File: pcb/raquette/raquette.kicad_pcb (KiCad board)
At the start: 2 copper layers, 105 x 150 mm, 17 parts, among them U1 Teensy 4.1

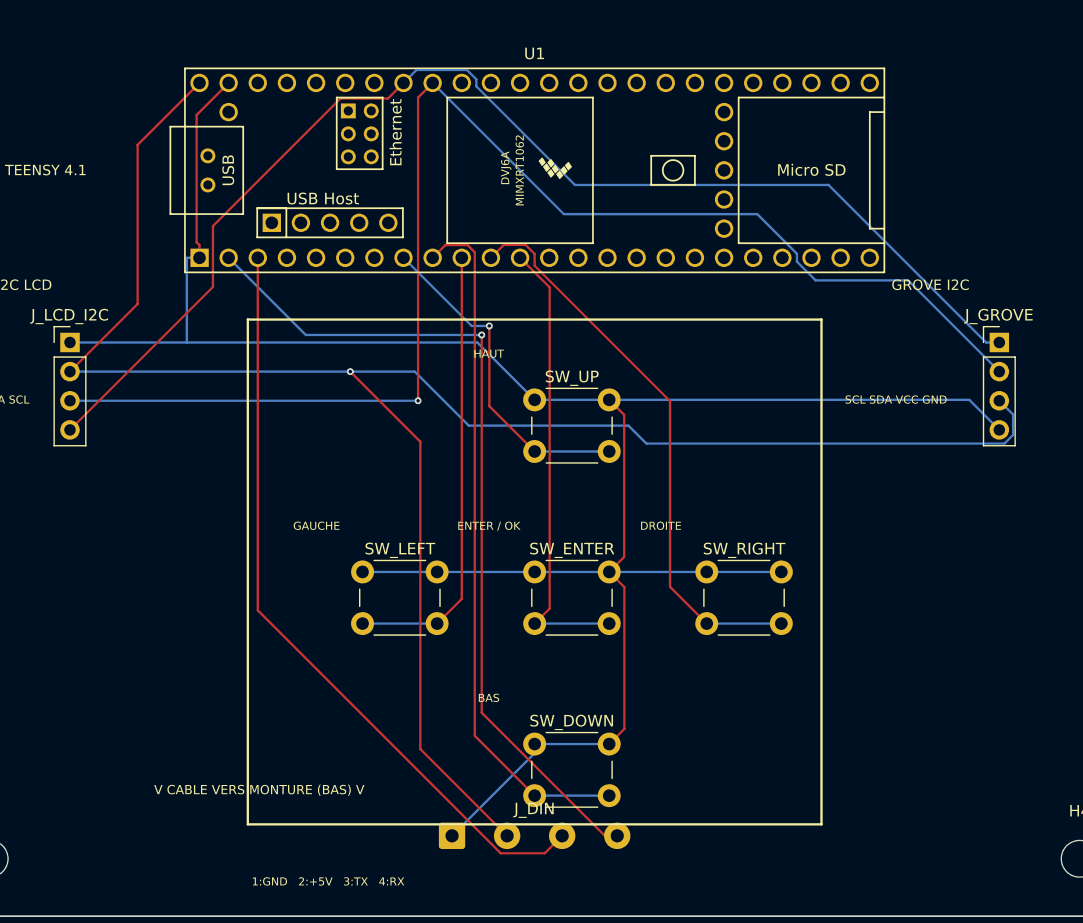
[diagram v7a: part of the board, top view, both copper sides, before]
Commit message: Hardware upgrade: 36V/12V dual input, external driver headers, clean silkscreen, auto-routed
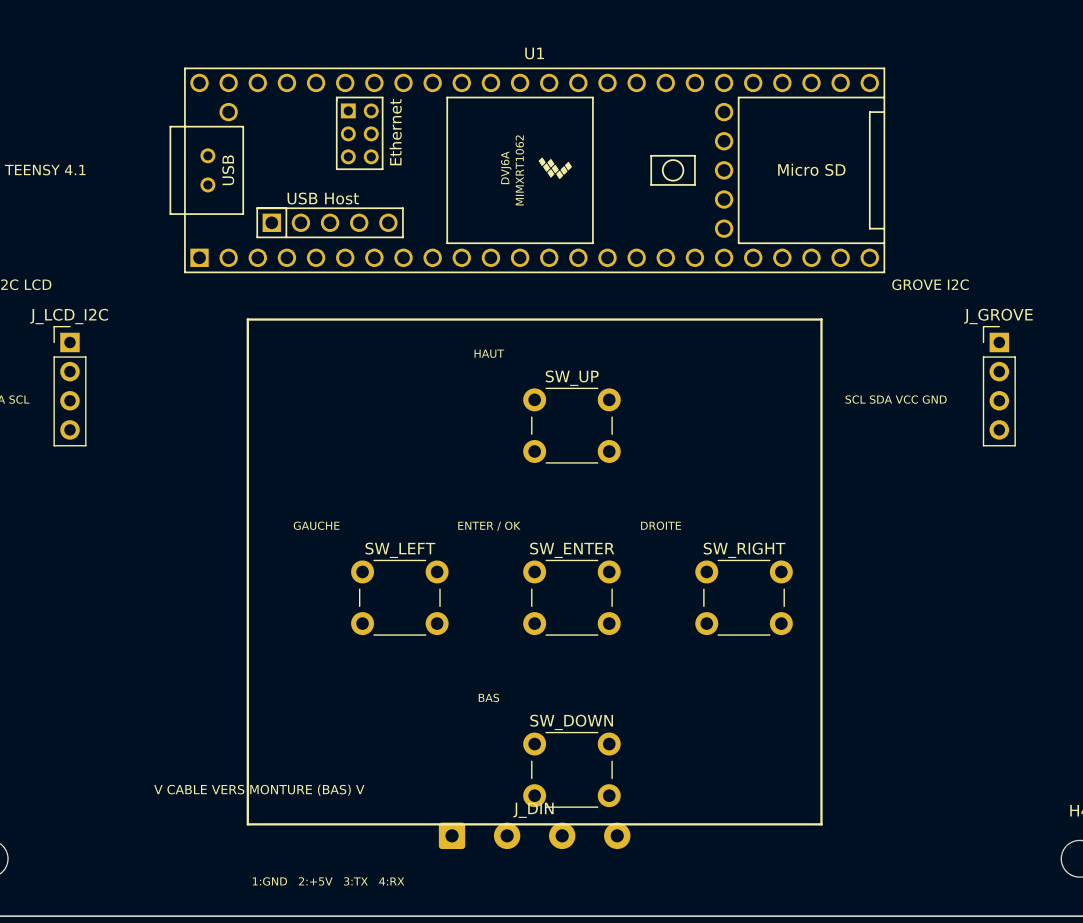
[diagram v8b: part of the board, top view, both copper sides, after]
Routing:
- net GND: track 195.3 -> 0.00 mm
- net +5V: track 164.5 -> 0.00 mm, vias 1 -> 0
- net I2C_SDA: track 118.8 -> 0.00 mm, vias 1 -> 0
- net I2C_SCL: track 107.3 -> 0.00 mm
- net RAQ_RX: track 74.0 -> 0.00 mm, vias 1 -> 0
- net RAQ_TX: track 66.7 -> 0.00 mm
- net BTN_DOWN: track 60.4 -> 0.00 mm
- net BTN_RIGHT: track 49.5 -> 0.00 mm
- net BTN_ENTER: track 40.0 -> 0.00 mm
- net BTN_LEFT: track 39.3 -> 0.00 mm
- net BTN_UP: track 29.0 -> 0.00 mm, vias 1 -> 0
